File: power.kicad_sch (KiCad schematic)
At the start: 12 parts, among them U3 AP64501

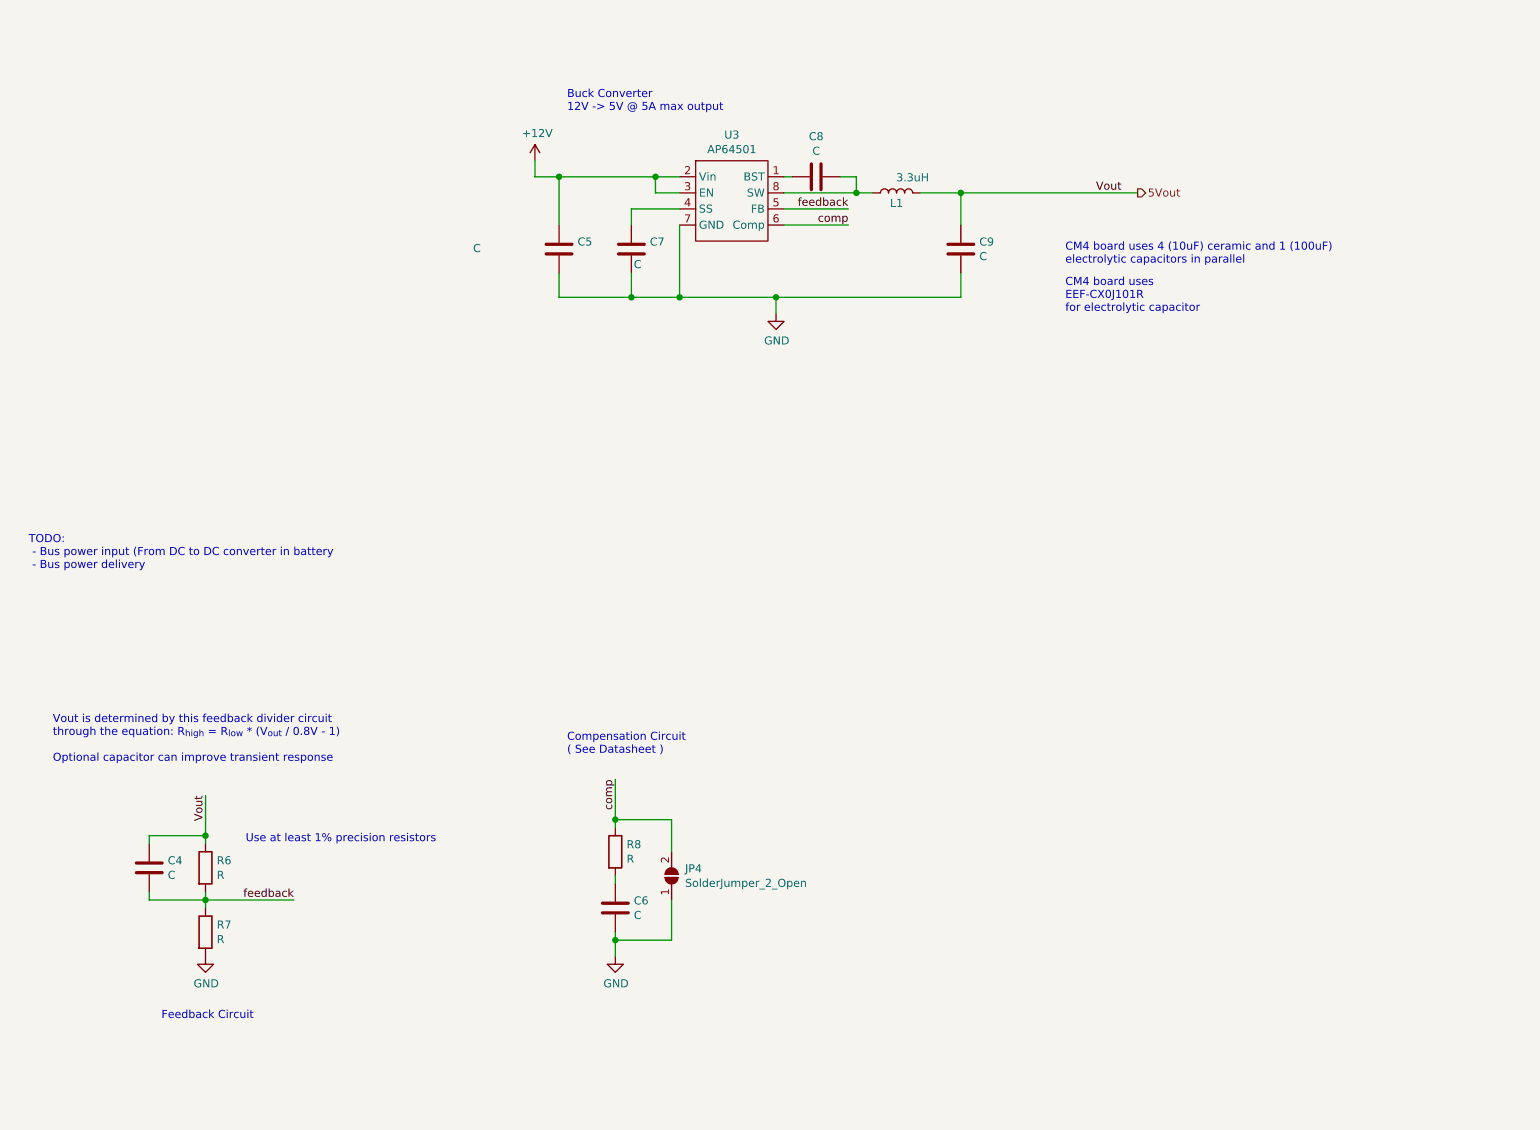
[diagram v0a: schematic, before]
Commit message: more layout: power supply and gpio
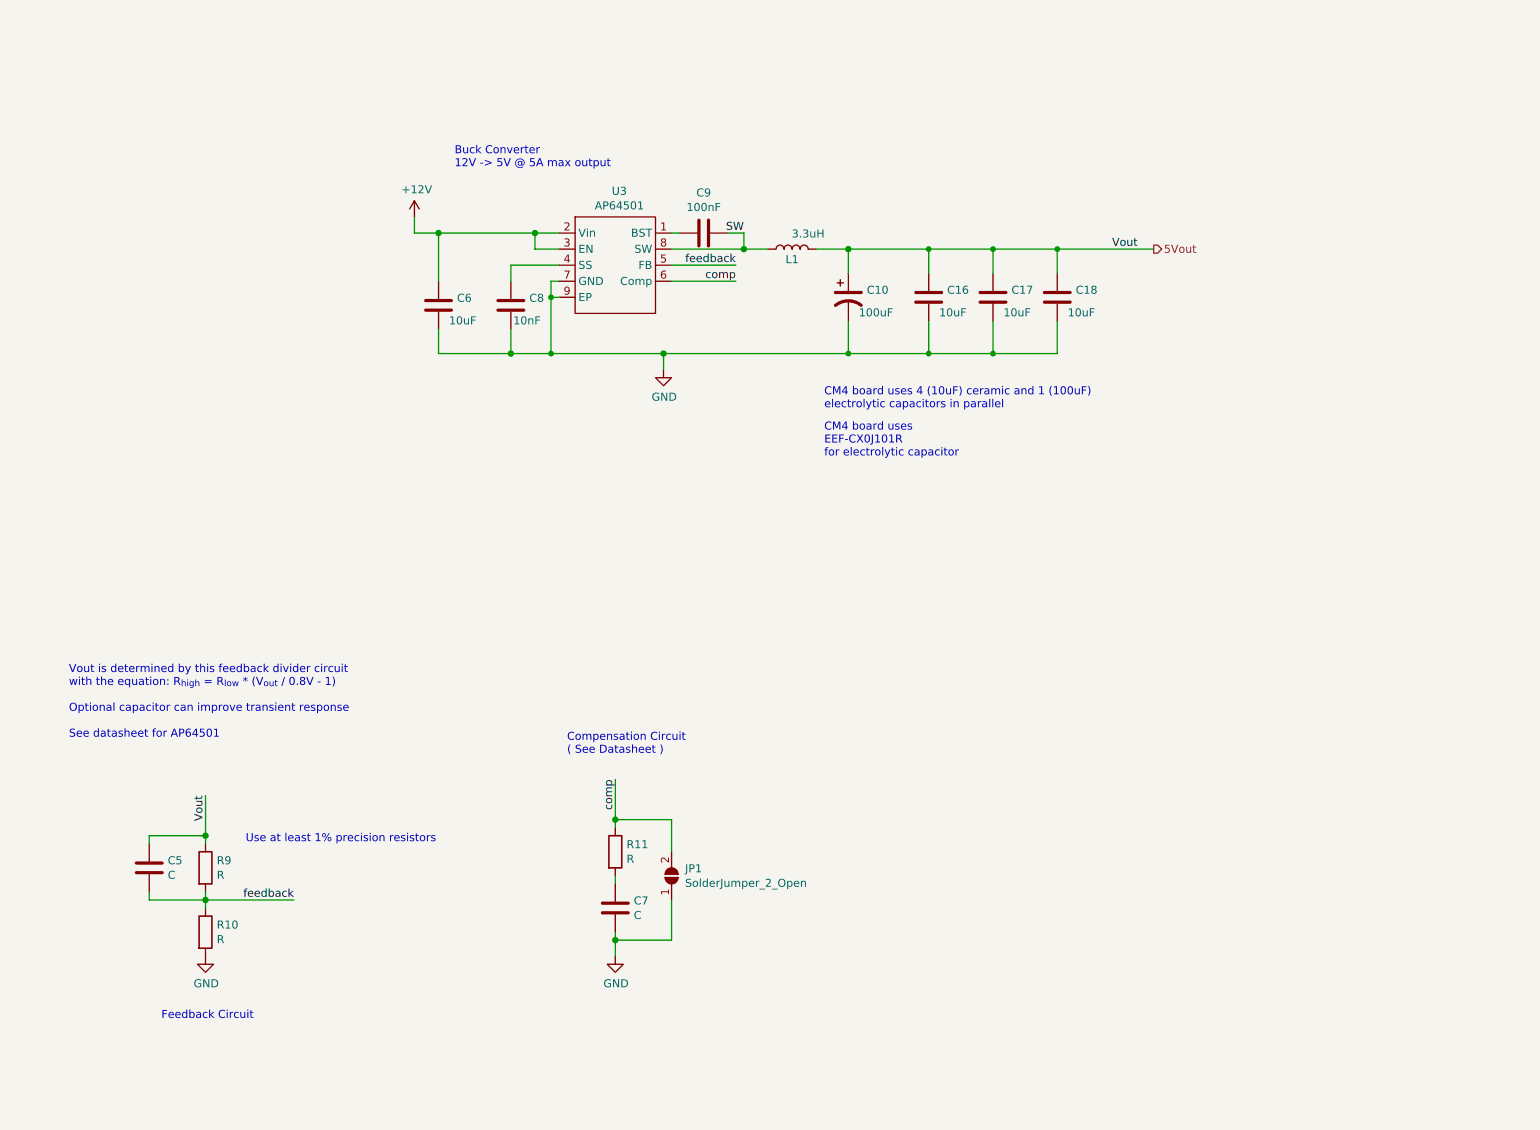
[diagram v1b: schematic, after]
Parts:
- removed C5, C9: C, symbol Device:C
- added C10: 100uF, Capacitor_SMD:CP_Elec_6.3x5.9, symbol symbols:100uF
- added C16, C17, C18, C6: 10uF, Capacitor_SMD:C_0805_2012Metric, symbol symbols:CAP-CERAMIC-10uF
- C8: renamed from C7; value C -> 10nF
- C9: renamed from C8; value C -> 100nF
- L1: footprint (none) -> Custom-Footprints:Bourns SRN6045Y Inductor
- renumbered C4 to C5, C6 to C7, JP4 to JP1, R7 to R10, R8 to R11, R6 to R9
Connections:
- net +12V: now also C6.1
- net 5Vout: now also C10.1, C16.1, C17.1, C18.1
- net GND: now also U3.9 (EP), C10.2, C16.2, C17.2, C18.2, C6.2
- net SW: now reaches C9.2, L1.1, U3.8 (SW)
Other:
- note added: "Vout is determined by this feedback divider circuit with the equation: R_{high} = R_{low} * (V_{out} / 0.8V - 1) Optional capacitor can improve transient response See datasheet for AP64501"
- note removed: "TODO: - Bus power input (From DC to DC converter in battery - Bus power delivery"
- note removed: "Vout is determined by this feedback divider circuit through the equation: R_{high} = R_{low} * (V_{out} / 0.8V - 1) Optional capacitor can improve transient response"
- moved on the sheet: C8, C9, L1

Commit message: Finished trace routing
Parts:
- C10: renamed from C6; value 10uF -> CAP-CERAMIC-10uF
- C11: renamed from C8; value 10nF -> C
- C13: renamed from C9; value 100nF -> C
- C15: renamed from C16; value 10uF -> CAP-CERAMIC-10uF
- C16: renamed from C17; value 10uF -> CAP-CERAMIC-10uF
- C17: renamed from C18; value 10uF -> CAP-CERAMIC-10uF
- renumbered C7 to C12, C10 to C14, C5 to C9, JP1 to JP2, R9 to R18, R10 to R19, R11 to R20, U3 to U4
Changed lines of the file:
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@@
   (symbol (lib_id "power:+12V") (at 82.55 55.88 0) (unit 1)
     (in_bom yes) (on_board yes)
-    (property "Reference" "#PWR0140" (id 0) (at 82.55 59.69 0)
+    (property "Reference" "#PWR0158" (id 0) (at 82.55 59.69 0)
       (effects (font (size 1.27 1.27)) hide)
     )
@@
   (symbol (lib_id "power:GND") (at 49.53 172.72 0) (unit 1)
     (in_bom yes) (on_board yes)
-    (property "Reference" "#PWR0137" (id 0) (at 49.53 179.07 0)
+    (property "Reference" "#PWR0155" (id 0) (at 49.53 179.07 0)
       (effects (font (size 1.27 1.27)) hide)
     )
@@
   (symbol (lib_id "power:GND") (at 114.3 172.72 0) (unit 1)
     (in_bom yes) (on_board yes)
-    (property "Reference" "#PWR0138" (id 0) (at 114.3 179.07 0)
+    (property "Reference" "#PWR0156" (id 0) (at 114.3 179.07 0)
       (effects (font (size 1.27 1.27)) hide)
     )
@@
   (symbol (lib_id "power:GND") (at 121.92 80.01 0) (unit 1)
     (in_bom yes) (on_board yes)
-    (property "Reference" "#PWR0139" (id 0) (at 121.92 86.36 0)
+    (property "Reference" "#PWR0157" (id 0) (at 121.92 86.36 0)
       (effects (font (size 1.27 1.27)) hide)
     )
@@
   (symbol (lib_id "Device:R") (at 49.53 158.75 0) (unit 1)
     (in_bom yes) (on_board yes)
-    (property "Reference" "R9" (id 0) (at 51.3081 157.6006 0)
+    (property "Reference" "R18" (id 0) (at 51.3081 157.6006 0)
       (effects (font (size 1.27 1.27)) (justify left))
     )
@@
   (symbol (lib_id "Device:R") (at 49.53 168.91 0) (unit 1)
     (in_bom yes) (on_board yes)
-    (property "Reference" "R10" (id 0) (at 51.3081 167.7606 0)
+    (property "Reference" "R19" (id 0) (at 51.3081 167.7606 0)
       (effects (font (size 1.27 1.27)) (justify left))
     )
@@
   (symbol (lib_id "Device:R") (at 114.3 156.21 0) (unit 1)
     (in_bom yes) (on_board yes)
-    (property "Reference" "R11" (id 0) (at 116.0781 155.0606 0)
+    (property "Reference" "R20" (id 0) (at 116.0781 155.0606 0)
       (effects (font (size 1.27 1.27)) (justify left))
     )
@@
   (symbol (lib_id "Jumper:SolderJumper_2_Open") (at 123.19 160.02 90) (unit 1)
     (in_bom yes) (on_board yes)
-    (property "Reference" "JP1" (id 0) (at 125.3237 158.8706 90)
+    (property "Reference" "JP2" (id 0) (at 125.3237 158.8706 90)
       (effects (font (size 1.27 1.27)) (justify right))
     )
@@
   (symbol (lib_id "Device:C") (at 40.64 158.75 0) (unit 1)
     (in_bom yes) (on_board yes)
-    (property "Reference" "C5" (id 0) (at 43.5611 157.6006 0)
+    (property "Reference" "C9" (id 0) (at 43.5611 157.6006 0)
       (effects (font (size 1.27 1.27)) (justify left))
     )
@@
   (symbol (lib_id "symbols:CAP-CERAMIC-10uF") (at 86.36 69.85 0) (unit 1)
     (in_bom yes) (on_board yes)
-    (property "Reference" "C6" (id 0) (at 89.2811 68.7006 0)
-      (effects (font (size 1.27 1.27)) (justify left))
-    )
-    (property "Value" "10uF" (id 1) (at 88.0111 72.2693 0)
+    (property "Reference" "C10" (id 0) (at 89.2811 68.7006 0)
+      (effects (font (size 1.27 1.27)) (justify left))
+    )
+    (property "Value" "CAP-CERAMIC-10uF" (id 1) (at 88.0111 72.2693 0)
       (effects (font (size 1.27 1.27)) (justify left))
     )
@@
   (symbol (lib_id "Device:C") (at 97.79 69.85 0) (unit 1)
     (in_bom yes) (on_board yes)
-    (property "Reference" "C8" (id 0) (at 100.7111 68.7006 0)
-      (effects (font (size 1.27 1.27)) (justify left))
-    )
-    (property "Value" "10nF" (id 1) (at 98.171 72.269 0)
+    (property "Reference" "C11" (id 0) (at 100.7111 68.7006 0)
+      (effects (font (size 1.27 1.27)) (justify left))
+    )
+    (property "Value" "C" (id 1) (at 98.171 72.269 0)
       (effects (font (size 1.27 1.27)) (justify left))
     )
@@
   (symbol (lib_id "Device:C") (at 114.3 165.1 0) (unit 1)
     (in_bom yes) (on_board yes)
-    (property "Reference" "C7" (id 0) (at 117.2211 163.9506 0)
+    (property "Reference" "C12" (id 0) (at 117.2211 163.9506 0)
       (effects (font (size 1.27 1.27)) (justify left))
     )
@@
   (symbol (lib_id "Device:C") (at 128.27 58.42 90) (unit 1)
     (in_bom yes) (on_board yes)
-    (property "Reference" "C9" (id 0) (at 128.27 52.0508 90))
-    (property "Value" "100nF" (id 1) (at 128.27 54.3495 90))
+    (property "Reference" "C13" (id 0) (at 128.27 52.0508 90))
+    (property "Value" "C" (id 1) (at 128.27 54.3495 90))
     (property "Footprint" "Capacitor_SMD:C_0805_2012Metric" (id 2) (at 132.08 57.4548 0)
       (effects (font (size 1.27 1.27)) hide)
@@
   (symbol (lib_id "symbols:100uF") (at 151.13 68.58 0) (unit 1)
     (in_bom yes) (on_board yes)
-    (property "Reference" "C10" (id 0) (at 154.0511 67.4306 0)
+    (property "Reference" "C14" (id 0) (at 154.0511 67.4306 0)
       (effects (font (size 1.27 1.27)) (justify left))
     )
@@
   (symbol (lib_id "symbols:CAP-CERAMIC-10uF") (at 163.83 68.58 0) (unit 1)
     (in_bom yes) (on_board yes)
-    (property "Reference" "C16" (id 0) (at 166.7511 67.4306 0)
-      (effects (font (size 1.27 1.27)) (justify left))
-    )
-    (property "Value" "10uF" (id 1) (at 165.4811 70.9993 0)
+    (property "Reference" "C15" (id 0) (at 166.7511 67.4306 0)
+      (effects (font (size 1.27 1.27)) (justify left))
+    )
+    (property "Value" "CAP-CERAMIC-10uF" (id 1) (at 165.4811 70.9993 0)
       (effects (font (size 1.27 1.27)) (justify left))
     )
@@
   (symbol (lib_id "symbols:CAP-CERAMIC-10uF") (at 173.99 68.58 0) (unit 1)
     (in_bom yes) (on_board yes)
-    (property "Reference" "C17" (id 0) (at 176.9111 67.4306 0)
-      (effects (font (size 1.27 1.27)) (justify left))
-    )
-    (property "Value" "10uF" (id 1) (at 175.641 70.999 0)
+    (property "Reference" "C16" (id 0) (at 176.9111 67.4306 0)
+      (effects (font (size 1.27 1.27)) (justify left))
+    )
+    (property "Value" "CAP-CERAMIC-10uF" (id 1) (at 175.641 70.999 0)
       (effects (font (size 1.27 1.27)) (justify left))
     )
@@
   (symbol (lib_id "symbols:CAP-CERAMIC-10uF") (at 184.15 68.58 0) (unit 1)
     (in_bom yes) (on_board yes)
-    (property "Reference" "C18" (id 0) (at 187.0711 67.4306 0)
-      (effects (font (size 1.27 1.27)) (justify left))
-    )
-    (property "Value" "10uF" (id 1) (at 185.801 70.999 0)
+    (property "Reference" "C17" (id 0) (at 187.0711 67.4306 0)
+      (effects (font (size 1.27 1.27)) (justify left))
+    )
+    (property "Value" "CAP-CERAMIC-10uF" (id 1) (at 185.801 70.999 0)
       (effects (font (size 1.27 1.27)) (justify left))
     )
@@
   (symbol (lib_id "symbols:AP64501") (at 114.3 62.23 0) (unit 1)
     (in_bom yes) (on_board yes)
-    (property "Reference" "U3" (id 0) (at 114.935 51.7965 0))
+    (property "Reference" "U4" (id 0) (at 114.935 51.7965 0))
     (property "Value" "AP64501" (id 1) (at 114.935 54.0952 0))
     (property "Footprint" "Package_SO:SOIC-8-1EP_3.9x4.9mm_P1.27mm_EP2.514x3.2mm" (id 2) (at 104.14 60.96 0)
